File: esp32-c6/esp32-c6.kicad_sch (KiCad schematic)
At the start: 1 part, among them U1 ESP32-C6

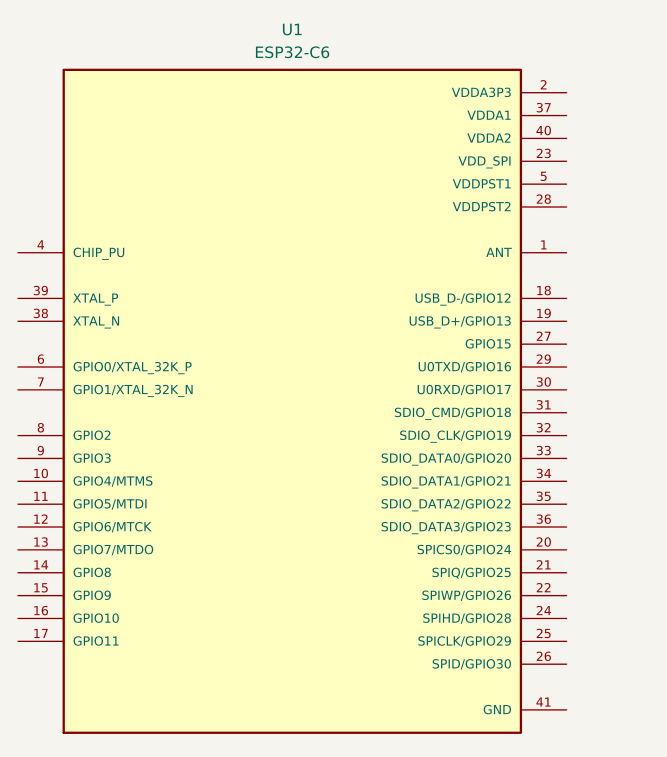
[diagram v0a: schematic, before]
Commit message: fix: use official espressif lib for esp32-c6 projects
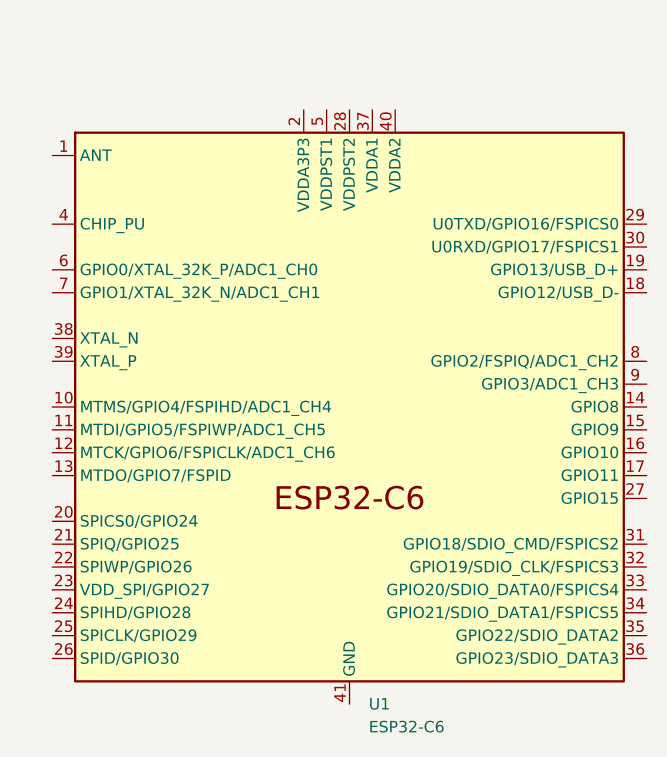
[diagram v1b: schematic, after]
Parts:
- removed U1: ESP32-C6, ESP32:ESP32-C6, symbol ESP32:ESP32-C6
- added U1: ESP32-C6, Package_DFN_QFN:QFN-40-1EP_5x5mm_P0.4mm_EP3.6x3.6mm, symbol PCM_Espressif:ESP32-C6
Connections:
- new net: U1.2 (VDDA3P3), U1.3 (VDDA3P3)
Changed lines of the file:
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@@
 	(paper "A4")
 	(symbol
-		(lib_id "ESP32:ESP32-C6")
-		(at 143.51 93.345 0)
+		(lib_id "PCM_Espressif:ESP32-C6")
+		(at 149.86 95.25 0)
 		(unit 1)
 		(exclude_from_sim no)
@@
 		(fields_autoplaced yes)
 		(property "Reference" "U1"
-			(at 143.51 53.34 0)
+			(at 152.0033 128.27 0)
 			(effects
 				(font
 					(size 1.27 1.27)
 				)
+				(justify left)
 			)
 		)
 		(property "Value" "ESP32-C6"
-			(at 143.51 55.88 0)
+			(at 152.0033 130.81 0)
 			(effects
 				(font
 					(size 1.27 1.27)
 				)
+				(justify left)
 			)
 		)
-		(property "Footprint" "ESP32:ESP32-C6"
-			(at 143.51 93.345 0)
-			(effects
-				(font
-					(size 1.27 1.27)
-				)
-				(justify bottom)
-				(hide yes)
-			)
-		)
-		(property "Datasheet" ""
-			(at 143.51 93.345 0)
+		(property "Footprint" "Package_DFN_QFN:QFN-40-1EP_5x5mm_P0.4mm_EP3.6x3.6mm"
+			(at 149.86 135.89 0)
 			(effects
 				(font
@@
 			)
 		)
-		(property "Description" ""
-			(at 143.51 93.345 0)
+		(property "Datasheet" "https://www.espressif.com/sites/default/files/documentation/esp32-c6_datasheet_en.pdf"
+			(at 152.4 138.43 0)
 			(effects
 				(font
@@
 			)
 		)
-		(property "MF" "Espressif Systems"
-			(at 143.51 93.345 0)
+		(property "Description" "ESP32C6,ultra-low-power SoC with RISC-V single-core microprocessor,2.4 GHz Wi-Fi 6 (802.11 ax), Bluetooth 5 (LE), Zigbee and Thread (802.15.4),QFN-40"
+			(at 149.86 95.25 0)
 			(effects
 				(font
 					(size 1.27 1.27)
 				)
-				(justify bottom)
 				(hide yes)
 			)
 		)
-		(property "MAXIMUM_PACKAGE_HEIGHT" "0.9mm"
-			(at 143.51 93.345 0)
-			(effects
-				(font
-					(size 1.27 1.27)
-				)
-				(justify bottom)
-				(hide yes)
-			)
+		(pin "1"
 		)
-		(property "Package" "None"
-			(at 143.51 93.345 0)
-			(effects
-				(font
-					(size 1.27 1.27)
-				)
-				(justify bottom)
-				(hide yes)
-			)
+		(pin "6"
 		)
-		(property "Price" "None"
-			(at 143.51 93.345 0)
-			(effects
-				(font
-					(size 1.27 1.27)
-				)
-				(justify bottom)
-				(hide yes)
-			)
+		(pin "4"
 		)
-		(property "Check_prices" "https://www.snapeda.com/parts/ESP32-C6/Espressif+Systems/view-part/?ref=eda"
-			(at 143.51 93.345 0)
-			(effects
-				(font
-					(size 1.27 1.27)
-				)
-				(justify bottom)
-				(hide yes)
-			)
+		(pin "25"
 		)
-		(property "STANDARD" "IPC-7351B"
-			(at 143.51 93.345 0)
-			(effects
-				(font
-					(size 1.27 1.27)
-				)
-				(justify bottom)
-				(hide yes)
-			)
+		(pin "40"
 		)
-		(property "PARTREV" "v0.5"
-			(at 143.51 93.345 0)
-			(effects
-				(font
-					(size 1.27 1.27)
-				)
-				(justify bottom)
-				(hide yes)
-			)
+		(pin "30"
 		)
-		(property "SnapEDA_Link" "https://www.snapeda.com/parts/ESP32-C6/Espressif+Systems/view-part/?ref=snap"
-			(at 143.51 93.345 0)
-			(effects
-				(font
-					(size 1.27 1.27)
-				)
-				(justify bottom)
-				(hide yes)
-			)
+		(pin "18"
 		)
-		(property "MP" "ESP32-C6"
-			(at 143.51 93.345 0)
-			(effects
-				(font
-					(size 1.27 1.27)
-				)
-				(justify bottom)
-				(hide yes)
-			)
+		(pin "9"
 		)
-		(property "Purchase-URL" "https://www.snapeda.com/api/url_track_click_mouser/?unipart_id=13539068&manufacturer=Espressif Systems&part_name=ESP32-C6&search_term=None"
-			(at 143.51 93.345 0)
-			(effects
-				(font
-					(size 1.27 1.27)
-				)
-				(justify bottom)
-				(hide yes)
-			)
+		(pin "24"
 		)
-		(property "Description_1" "IC RF TxRx + MCU Bluetooth, WiFi Bluetooth v5.0, Thread, Zigbee® 2.412GHz ~ 2.484GHz 40-VFQFN Exposed Pad"
-			(at 143.51 93.345 0)
-			(effects
-				(font
-					(size 1.27 1.27)
-				)
-				(justify bottom)
-				(hide yes)
-			)
+		(pin "38"
 		)
-		(property "MANUFACTURER" "Espressif Systems"
-			(at 143.51 93.345 0)
-			(effects
-				(font
-					(size 1.27 1.27)
-				)
-				(justify bottom)
-				(hide yes)
-			)
+		(pin "22"
 		)
-		(property "Availability" "In Stock"
-			(at 143.51 93.345 0)
-			(effects
-				(font
-					(size 1.27 1.27)
-				)
-				(justify bottom)
-				(hide yes)
-			)
+		(pin "12"
 		)
-		(property "SNAPEDA_PN" "ESP32-C6"
-			(at 143.51 93.345 0)
-			(effects
-				(font
-					(size 1.27 1.27)
-				)
-				(justify bottom)
-				(hide yes)
-			)
+		(pin "23"
+		)
+		(pin "5"
+		)
+		(pin "20"
+		)
+		(pin "13"
+		)
+		(pin "10"
+		)
+		(pin "21"
+		)
+		(pin "26"
+		)
+		(pin "39"
+		)
+		(pin "2"
+		)
+		(pin "11"
+		)
+		(pin "28"
+		)
+		(pin "41"
+		)
+		(pin "3"
+		)
+		(pin "7"
+		)
+		(pin "37"
+		)
+		(pin "29"
+		)
+		(pin "19"
+		)
+		(pin "8"
+		)
+		(pin "14"
+		)
+		(pin "27"
+		)
+		(pin "16"
+		)
+		(pin "31"
 		)
 		(pin "32"
 		)
-		(pin "16"
-		)
-		(pin "34"
-		)
-		(pin "24"
-		)
-		(pin "14"
-		)
-		(pin "41"
+		(pin "17"
 		)
 		(pin "33"
 		)
-		(pin "21"
-		)
-		(pin "20"
-		)
-		(pin "23"
-		)
 		(pin "15"
-		)
-		(pin "1"
-		)
-		(pin "2"
-		)
-		(pin "5"
-		)
-		(pin "28"
-		)
-		(pin "30"
-		)
-		(pin "40"
-		)
-		(pin "31"
-		)
-		(pin "27"
-		)
-		(pin "37"
-		)
-		(pin "18"
-		)
-		(pin "3"
-		)
-		(pin "17"
-		)
-		(pin "19"
-		)
-		(pin "29"
 		)
 		(pin "35"
@@
 		(pin "36"
 		)
-		(pin "22"
-		)
-		(pin "25"
-		)
-		(pin "26"
-		)
-		(pin "12"
-		)
-		(pin "39"
-		)
-		(pin "38"
-		)
-		(pin "6"
-		)
-		(pin "9"
-		)
-		(pin "13"
-		)
-		(pin "4"
-		)
-		(pin "7"
-		)
-		(pin "8"
-		)
-		(pin "10"
-		)
-		(pin "11"
+		(pin "34"
 		)
 		(instances
 			(project ""
-				(path "/36cb6903-3d20-46f4-b437-0a11aebeacb9"
+				(path "/198533c0-455e-45b0-845a-821d8f7e55d4"
 					(reference "U1")
 					(unit 1)
